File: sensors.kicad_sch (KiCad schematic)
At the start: 42 parts, among them IC2 ACS37800KMACTR-030B3-SPI, IC3 ACS37800KMACTR-030B3-SPI, IC4 ACS37800KMACTR-030B3-SPI, U3 UA9637A, U5 UA9637A, U7 UA9637A

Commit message: feat: production codes
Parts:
- IC2, IC3, IC4: LCSC (none) -> C5576508
- U3, U5, U7: LCSC (none) -> C434452
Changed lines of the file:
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@@
 			)
 		)
+		(property "LCSC" "C434452"
+			(at 101.6 242.57 0)
+			(effects
+				(font
+					(size 1.27 1.27)
+				)
+				(hide yes)
+			)
+		)
 		(pin "1"
 		)
@@
 			)
 		)
+		(property "LCSC" "C434452"
+			(at 280.67 172.72 0)
+			(effects
+				(font
+					(size 1.27 1.27)
+				)
+				(hide yes)
+			)
+		)
 		(pin "1"
 		)
@@
 			)
 		)
+		(property "LCSC" "C5576508"
+			(at 269.24 102.87 0)
+			(effects
+				(font
+					(size 1.27 1.27)
+				)
+				(hide yes)
+			)
+		)
 		(pin "5"
 		)
@@
 			)
 		)
+		(property "LCSC" "C434452"
+			(at 101.6 109.22 0)
+			(effects
+				(font
+					(size 1.27 1.27)
+				)
+				(hide yes)
+			)
+		)
 		(pin "1"
 		)
@@
 			)
 		)
+		(property "LCSC" "C5576508"
+			(at 88.9 172.72 0)
+			(effects
+				(font
+					(size 1.27 1.27)
+				)
+				(hide yes)
+			)
+		)
 		(pin "5"
 		)
@@
 				(hide yes)
 			)
+		)
+		(property "LCSC" "C5576508"
+			(at 91.44 33.02 0)
+			(effects
+				(font
+					(size 1.27 1.27)
+				)
+				(hide yes)
+			)

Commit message: fix: root sheet LCSC codes
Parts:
- C30, C31, C37, C38, C44, C45: LCSC (none) -> C1589
- C32, C33, C34, C39, C40, C47: LCSC (none) -> C14663
- R13, R14, R35, R36, R49, R50: LCSC (none) -> C177328
- R15, R16, R37, R38, R51, R52: LCSC (none) -> C4177
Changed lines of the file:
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@@
 			)
 		)
+		(property "LCSC" "C1589"
+			(at 254 187.96 0)
+			(effects
+				(font
+					(size 1.27 1.27)
+				)
+				(hide yes)
+			)
+		)
 		(pin "1"
 		)
@@
 			)
 		)
+		(property "LCSC" "C4177"
+			(at 298.45 167.64 90)
+			(effects
+				(font
+					(size 1.27 1.27)
+				)
+				(hide yes)
+			)
+		)
 		(pin "1"
 		)
@@
 			)
 		)
+		(property "LCSC" "C177328"
+			(at 69.85 78.74 0)
+			(effects
+				(font
+					(size 1.27 1.27)
+				)
+				(hide yes)
+			)
+		)
 		(pin "1"
 		)
@@
 			)
 		)
+		(property "LCSC" "C14663"
+			(at 138.43 171.45 0)
+			(effects
+				(font
+					(size 1.27 1.27)
+				)
+				(hide yes)
+			)
+		)
 		(pin "1"
 		)
@@
 			)
 		)
+		(property "LCSC" "C4177"
+			(at 119.38 104.14 90)
+			(effects
+				(font
+					(size 1.27 1.27)
+				)
+				(hide yes)
+			)
+		)
 		(pin "1"
 		)
@@
 			)
 		)
+		(property "LCSC" "C14663"
+			(at 288.29 147.32 0)
+			(effects
+				(font
+					(size 1.27 1.27)
+				)
+				(hide yes)
+			)
+		)
 		(pin "1"
 		)
@@
 			)
 		)
+		(property "LCSC" "C14663"
+			(at 109.22 217.17 0)
+			(effects
+				(font
+					(size 1.27 1.27)
+				)
+				(hide yes)
+			)
+		)
 		(pin "1"
 		)
@@
 			)
 		)
+		(property "LCSC" "C1589"
+			(at 74.93 124.46 0)
+			(effects
+				(font
+					(size 1.27 1.27)
+				)
+				(hide yes)
+			)
+		)
 		(pin "1"
 		)
@@
 			)
 		)
+		(property "LCSC" "C1589"
+			(at 248.92 149.86 0)
+			(effects
+				(font
+					(size 1.27 1.27)
+				)
+				(hide yes)
+			)
+		)
 		(pin "1"
 		)
@@
 			)
 		)
+		(property "LCSC" "C1589"
+			(at 74.93 257.81 0)
+			(effects
+				(font
+					(size 1.27 1.27)
+				)
+				(hide yes)
+			)
+		)
 		(pin "1"
 		)
@@
 			)
 		)
+		(property "LCSC" "C177328"
+			(at 69.85 212.09 0)
+			(effects
+				(font
+					(size 1.27 1.27)
+				)
+				(hide yes)
+			)
+		)
 		(pin "1"
 		)
@@
 			)
 		)
+		(property "LCSC" "C14663"
+			(at 318.77 101.6 0)
+			(effects
+				(font
+					(size 1.27 1.27)
+				)
+				(hide yes)
+			)
+		)
 		(pin "1"
 		)
@@
 			)
 		)
+		(property "LCSC" "C4177"
+			(at 119.38 237.49 90)
+			(effects
+				(font
+					(size 1.27 1.27)
+				)
+				(hide yes)
+			)
+		)
 		(pin "1"
 		)
@@
 			)
 		)
+		(property "LCSC" "C4177"
+			(at 119.38 114.3 90)
+			(effects
+				(font
+					(size 1.27 1.27)
+				)
+				(hide yes)
+			)
+		)
 		(pin "1"
 		)
@@
 			)
 		)
+		(property "LCSC" "C14663"
+			(at 109.22 83.82 0)
+			(effects
+				(font
+					(size 1.27 1.27)
+				)
+				(hide yes)
+			)
+		)
 		(pin "1"
 		)
@@
 			)
 		)
+		(property "LCSC" "C4177"
+			(at 119.38 247.65 90)
+			(effects
+				(font
+					(size 1.27 1.27)
+				)
+				(hide yes)
+			)
+		)
 		(pin "1"
 		)
@@
 			)
 		)
+		(property "LCSC" "C177328"
+			(at 254 180.34 0)
+			(effects
+				(font
+					(size 1.27 1.27)
+				)
+				(hide yes)
+			)
+		)
 		(pin "1"
 		)
@@
 			)
 		)
+		(property "LCSC" "C4177"
+			(at 298.45 177.8 90)
+			(effects
+				(font
+					(size 1.27 1.27)
+				)
+				(hide yes)
+			)
+		)
 		(pin "1"
 		)
@@
 			)
 		)
+		(property "LCSC" "C14663"
+			(at 140.97 31.75 0)
+			(effects
+				(font
+					(size 1.27 1.27)
+				)
+				(hide yes)
+			)
+		)
 		(pin "1"
 		)
@@
 			)
 		)
+		(property "LCSC" "C177328"
+			(at 74.93 116.84 0)
+			(effects
+				(font
+					(size 1.27 1.27)
+				)
+				(hide yes)
+			)
+		)
 		(pin "1"
 		)
@@
 			)
 		)
+		(property "LCSC" "C177328"
+			(at 248.92 142.24 0)
+			(effects
+				(font
+					(size 1.27 1.27)
+				)
+				(hide yes)
+			)
+		)
 		(pin "1"
 		)
@@
 			)
 		)
+		(property "LCSC" "C1589"
+			(at 69.85 219.71 0)
+			(effects
+				(font
+					(size 1.27 1.27)
+				)
+				(hide yes)
+			)
+		)
 		(pin "1"
 		)
@@
 			)
 		)
+		(property "LCSC" "C177328"
+			(at 74.93 250.19 0)
+			(effects
+				(font
+					(size 1.27 1.27)
+				)
+				(hide yes)
+			)
+		)
 		(pin "1"
 		)
@@
 			(at 69.85 86.36 0)
 			(effects
+				(font
+					(size 1.27 1.27)
+				)
+				(hide yes)
+			)
+		)
+		(property "LCSC" "C1589"
+			(at 69.85 86.36 0)
+			(effects

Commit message: feat: LCSC codes for all components to be soldered
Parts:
- C30, C31, C37, C38, C44, C45: LCSC C1589 -> C57112
- C35, C36, C42, C43, C49, C50: LCSC (none) -> C1603
- R13, R14, R35, R36, R49, R50: LCSC C177328 -> C22787
- R17, R18, R39, R40, R53, R54: LCSC (none) -> C22978
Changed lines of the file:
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@@
 			)
 		)
+		(property "LCSC" "C22978"
+			(at 124.46 119.38 0)
+			(effects
+				(font
+					(size 1.27 1.27)
+				)
+				(hide yes)
+			)
+		)
 		(pin "1"
 		)
@@
 			)
 		)
+		(property "LCSC" "C1603"
+			(at 144.78 119.38 0)
+			(effects
+				(font
+					(size 1.27 1.27)
+				)
+				(hide yes)
+			)
+		)
 		(pin "1"
 		)
@@
 			)
 		)
-		(property "LCSC" "C1589"
+		(property "LCSC" "C57112"
 			(at 254 187.96 0)
 			(effects
@@
 			)
 		)
-		(property "LCSC" "C177328"
+		(property "LCSC" "C22787"
 			(at 69.85 78.74 0)
 			(effects
@@
 			)
 		)
+		(property "LCSC" "C22978"
+			(at 133.35 252.73 0)
+			(effects
+				(font
+					(size 1.27 1.27)
+				)
+				(hide yes)
+			)
+		)
 		(pin "1"
 		)
@@
 			)
 		)
+		(property "LCSC" "C22978"
+			(at 124.46 252.73 0)
+			(effects
+				(font
+					(size 1.27 1.27)
+				)
+				(hide yes)
+			)
+		)
 		(pin "1"
 		)
@@
 			)
 		)
+		(property "LCSC" "C1603"
+			(at 335.28 182.88 0)
+			(effects
+				(font
+					(size 1.27 1.27)
+				)
+				(hide yes)
+			)
+		)
 		(pin "1"
 		)
@@
 			)
 		)
-		(property "LCSC" "C1589"
+		(property "LCSC" "C57112"
 			(at 74.93 124.46 0)
 			(effects
@@
 			)
 		)
-		(property "LCSC" "C1589"
+		(property "LCSC" "C57112"
 			(at 248.92 149.86 0)
 			(effects
@@
 			)
 		)
-		(property "LCSC" "C1589"
+		(property "LCSC" "C57112"
 			(at 74.93 257.81 0)
 			(effects
@@
 			)
 		)
-		(property "LCSC" "C177328"
+		(property "LCSC" "C22787"
 			(at 69.85 212.09 0)
 			(effects
@@
 			)
 		)
+		(property "LCSC" "C22978"
+			(at 312.42 182.88 0)
+			(effects
+				(font
+					(size 1.27 1.27)
+				)
+				(hide yes)
+			)
+		)
 		(pin "1"
 		)
@@
 			)
 		)
+		(property "LCSC" "C1603"
+			(at 144.78 252.73 0)
+			(effects
+				(font
+					(size 1.27 1.27)
+				)
+				(hide yes)
+			)
+		)
 		(pin "1"
 		)
@@
 			)
 		)
+		(property "LCSC" "C1603"
+			(at 323.85 182.88 0)
+			(effects
+				(font
+					(size 1.27 1.27)
+				)
+				(hide yes)
+			)
+		)
 		(pin "1"
 		)
@@
 			)
 		)
-		(property "LCSC" "C177328"
+		(property "LCSC" "C22787"
 			(at 254 180.34 0)
 			(effects
@@
 			)
 		)
+		(property "LCSC" "C22978"
+			(at 133.35 119.38 0)
+			(effects
+				(font
+					(size 1.27 1.27)
+				)
+				(hide yes)
+			)
+		)
 		(pin "1"
 		)
@@
 			)
 		)
+		(property "LCSC" "C1603"
+			(at 156.21 252.73 0)
+			(effects
+				(font
+					(size 1.27 1.27)
+				)
+				(hide yes)
+			)
+		)
 		(pin "1"
 		)
@@
 			)
 		)
-		(property "LCSC" "C177328"
+		(property "LCSC" "C22787"
 			(at 74.93 116.84 0)
 			(effects
@@
 			)
 		)
+		(property "LCSC" "C1603"
+			(at 156.21 119.38 0)
+			(effects
+				(font
+					(size 1.27 1.27)
+				)
+				(hide yes)
+			)
+		)
 		(pin "1"
 		)
@@
 			)
 		)
+		(property "LCSC" "C22978"
+			(at 303.53 182.88 0)
+			(effects
+				(font
+					(size 1.27 1.27)
+				)
+				(hide yes)
+			)
+		)
 		(pin "1"
 		)
@@
 			)
 		)
-		(property "LCSC" "C177328"
+		(property "LCSC" "C22787"
 			(at 248.92 142.24 0)
 			(effects
@@
 			)
 		)
-		(property "LCSC" "C1589"
+		(property "LCSC" "C57112"
 			(at 69.85 219.71 0)
 			(effects
@@
 			)
 		)
-		(property "LCSC" "C177328"
+		(property "LCSC" "C22787"
 			(at 74.93 250.19 0)
 			(effects
@@
 			)
 		)
-		(property "LCSC" "C1589"
+		(property "LCSC" "C57112"
 			(at 69.85 86.36 0)
 			(effects

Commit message: fix: prod notes
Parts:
- C32, C33, C34, C39, C40, C47: value 100n -> 100nF
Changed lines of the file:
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@@
 			)
 		)
-		(property "Value" "100n"
+		(property "Value" "100nF"
 			(at 144.78 172.72 0)
 			(effects
@@
 			)
 		)
-		(property "Value" "100n"
+		(property "Value" "100nF"
 			(at 294.64 148.59 0)
 			(effects
@@
 			)
 		)
-		(property "Value" "100n"
+		(property "Value" "100nF"
 			(at 115.57 218.44 0)
 			(effects
@@
 			)
 		)
-		(property "Value" "100n"
+		(property "Value" "100nF"
 			(at 325.12 102.87 0)
 			(effects
@@
 			)
 		)
-		(property "Value" "100n"
+		(property "Value" "100nF"
 			(at 115.57 85.09 0)
 			(effects
@@
 			)
 		)
-		(property "Value" "100n"
+		(property "Value" "100nF"
 			(at 147.32 33.02 0)
 			(effects

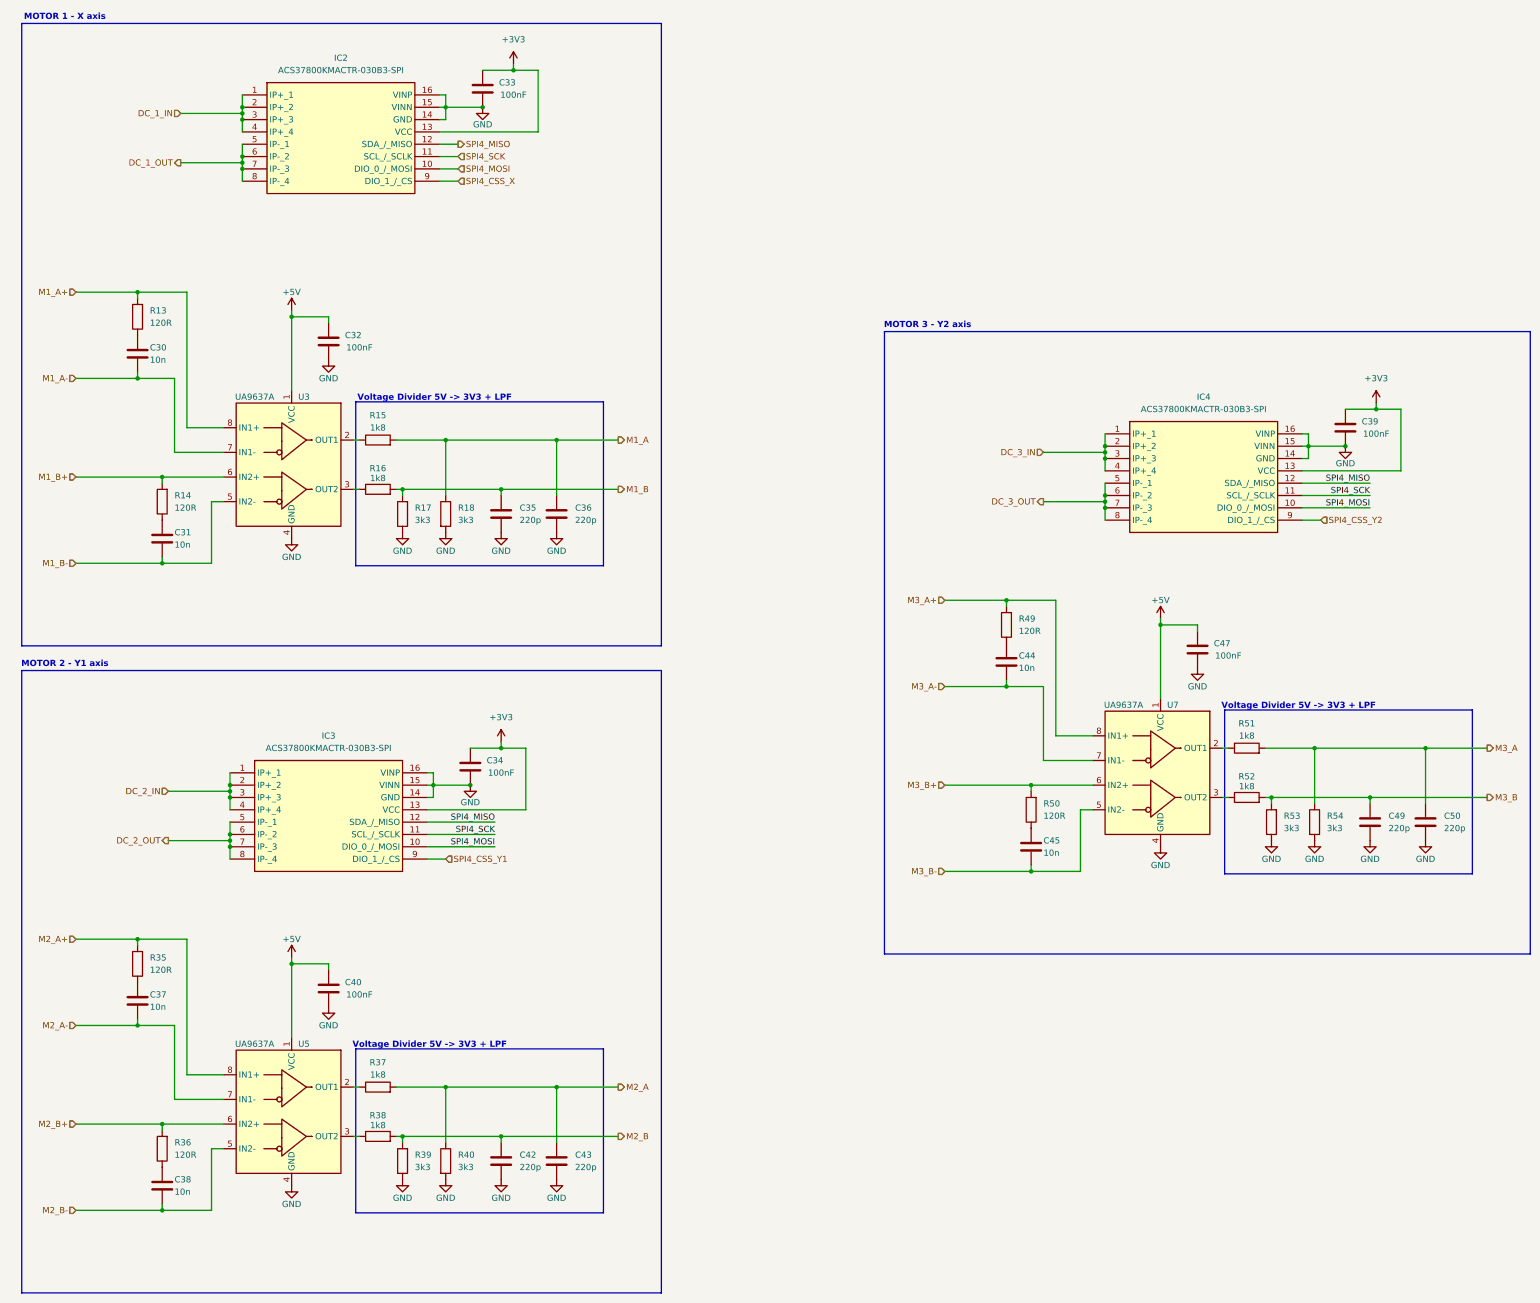
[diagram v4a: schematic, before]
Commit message: fix: DNP for current sensors
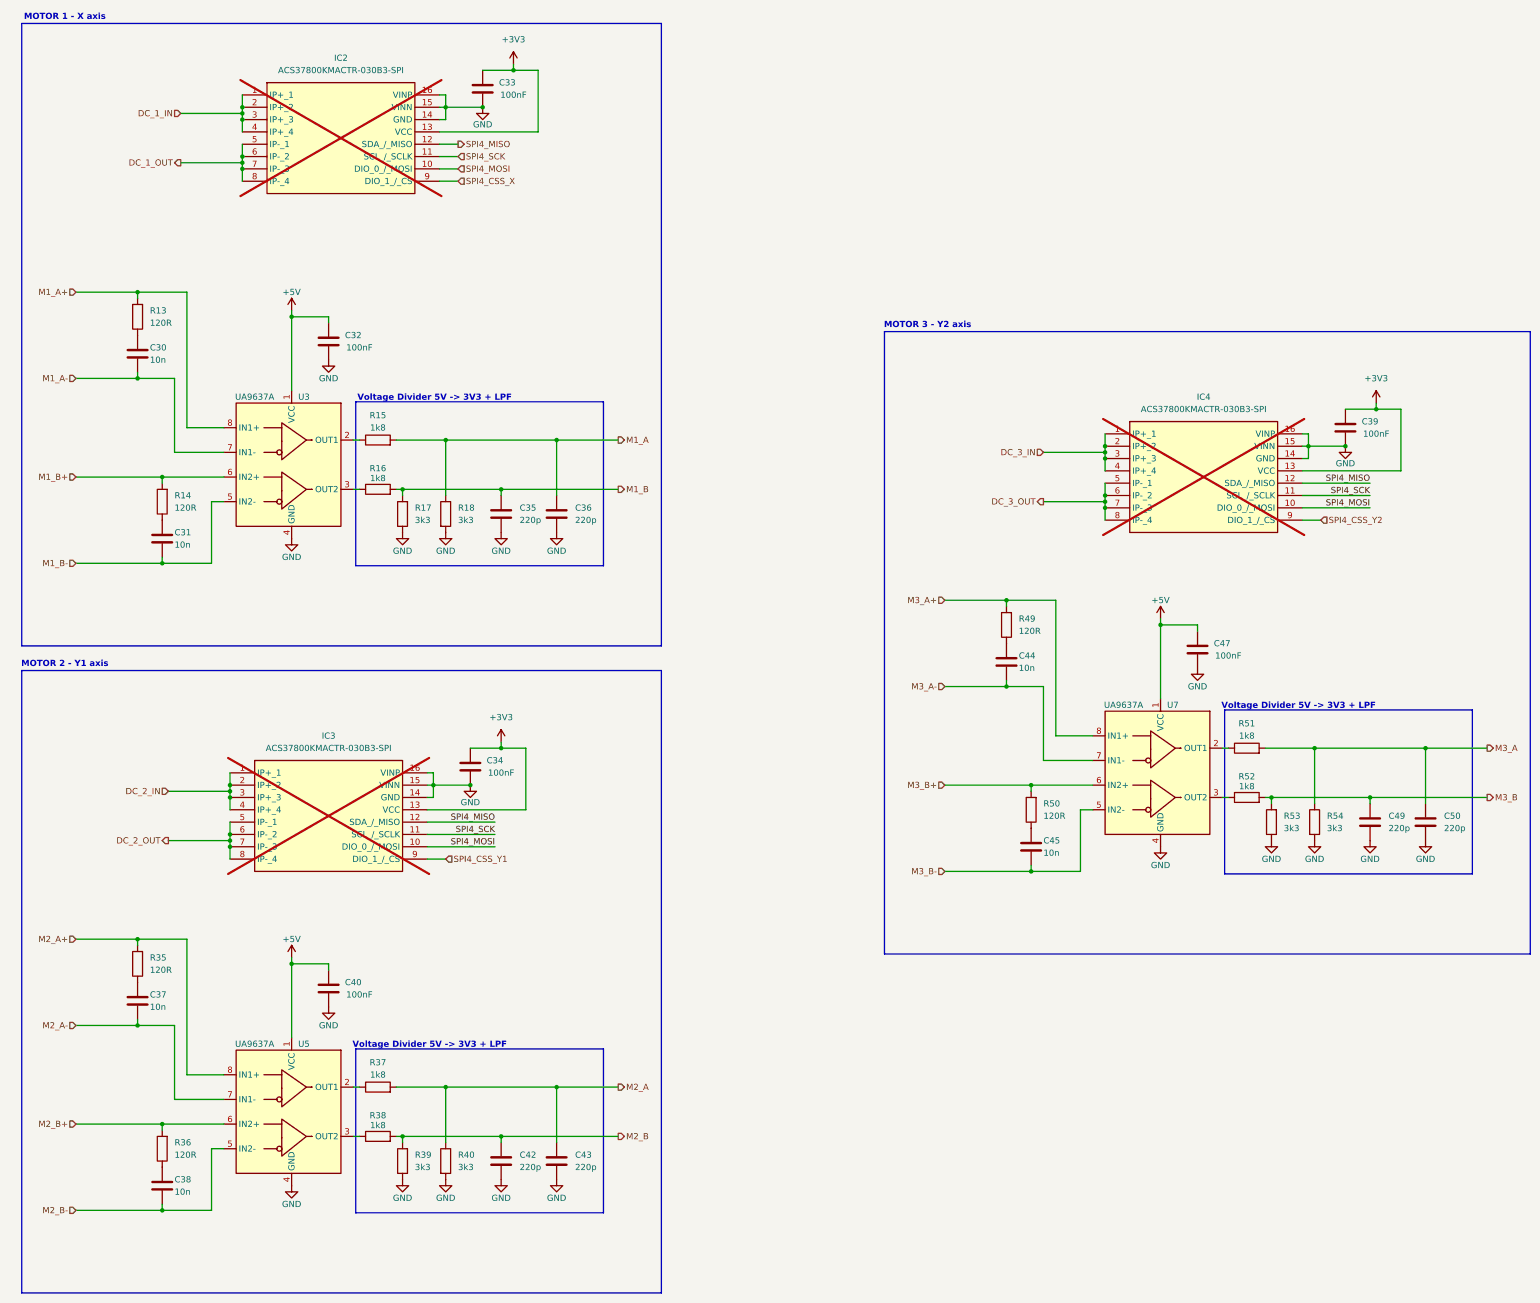
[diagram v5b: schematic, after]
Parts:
- IC2, IC3, IC4: now not fitted; now left out of the parts list
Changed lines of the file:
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@@
 		(unit 1)
 		(exclude_from_sim no)
-		(in_bom yes)
-		(on_board yes)
-		(dnp no)
+		(in_bom no)
+		(on_board yes)
+		(dnp yes)
 		(fields_autoplaced yes)
 		(property "Reference" "IC4"
@@
 		(unit 1)
 		(exclude_from_sim no)
-		(in_bom yes)
-		(on_board yes)
-		(dnp no)
+		(in_bom no)
+		(on_board yes)
+		(dnp yes)
 		(fields_autoplaced yes)
 		(property "Reference" "IC3"
@@
 		(unit 1)
 		(exclude_from_sim no)
-		(in_bom yes)
-		(on_board yes)
-		(dnp no)
+		(in_bom no)
+		(on_board yes)
+		(dnp yes)
 		(fields_autoplaced yes)
 		(property "Reference" "IC2"
